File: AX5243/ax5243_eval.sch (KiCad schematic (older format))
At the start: 29 parts, among them U1 AX5243-1-TA05, X1 12.000MHz, X2 SMA

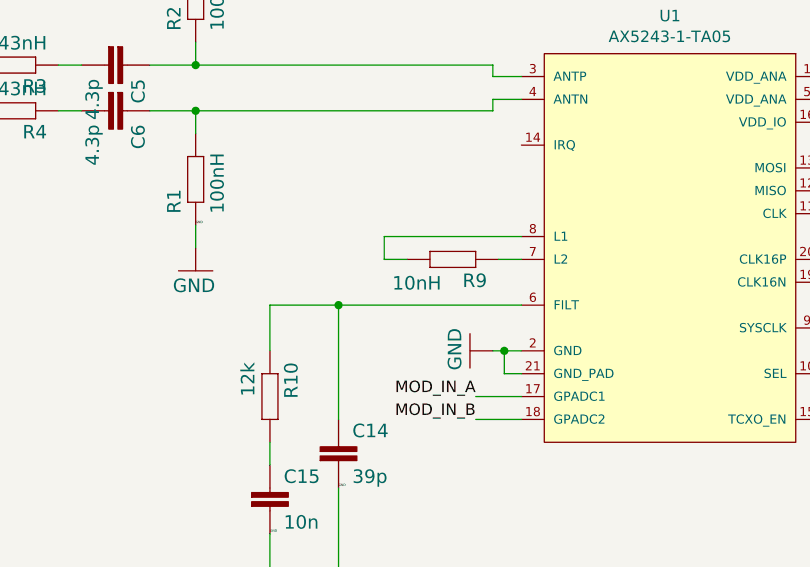
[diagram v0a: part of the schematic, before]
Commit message: Changed value of VCO coil inductor from 10nH to 6.8nH. Added BOM.
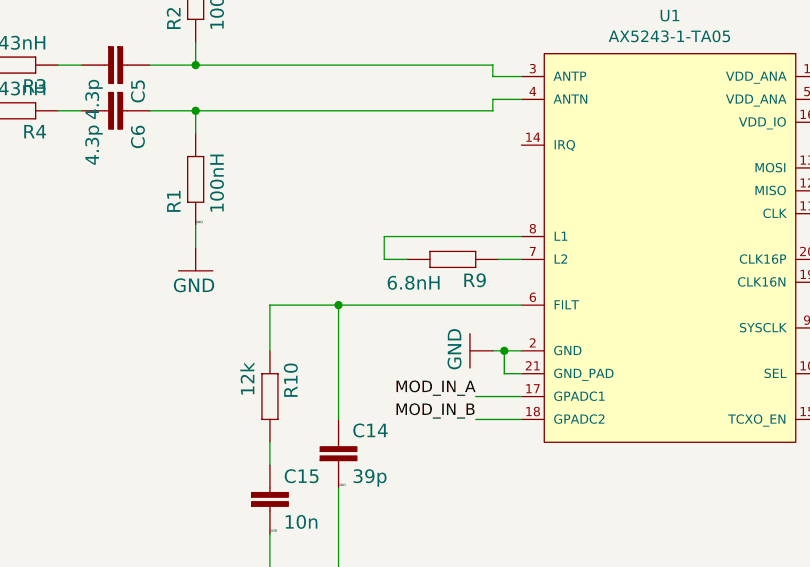
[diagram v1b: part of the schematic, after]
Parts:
- R9: value 10nH -> 6.8nH
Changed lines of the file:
@@
 P 5025 5100
 F 0 "R9" H 4875 5159 59  0000 L BNN
-F 1 "10nH" H 5075 5170 59  0000 L BNN
+F 1 "6.8nH" H 5075 5170 59  0000 L BNN
 F 2 "AX5043:R0603" H 5025 5100 50  0001 C CNN
 F 3 "" H 5025 5100 50  0001 C CNN
